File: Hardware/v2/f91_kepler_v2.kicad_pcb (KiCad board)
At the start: 2 copper layers, 30 x 28 mm, 89 parts, among them J1 LS013B7DH03 FPC, Q1 FS8205A, SW1 BTN1/BSL, SW2 BTN2, SW3 BTN3, U1 CC2652R7RGZ, U2 BQ51050B, U3 DW01A, U4 XC6206P302MR, U5 LIS2DW12, U6 DRV2605L, U7 ST25DV04K, Y1 48MHz FA-128, Y2 32.768kHz FC-135

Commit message: feat(hw/v2): geometry-driven placement engine — 0 copper shorts
Replace the fix2..fix5 hand-coordinate approach (could not converge on a
25x27mm / 89-footprint board) with a single authoritative placement engine
that uses real pad geometry headlessly.

Results (kicd-cli DRC, severity-error):
- shorting_items      78 -> 0
- solder_mask_bridge  88 -> 0
- copper_edge_clearance 7 -> 0
- inter-footprint clearance -> 0
- pad-bbox overlaps   90 -> 0
Remaining (non-fab-blocking): 12 intra-footprint clearance (U5 LGA + FL1
balun pins, part-intrinsic), 114 courtyards_overlap (informational),
202 unconnected (routing not started).

Engine: pin FIXED parts (MCU, LCD, edge buttons, antenna, battery, pogo
row), place movable ICs largest-first at nearest-free slot to a home hint,
then place each passive at the nearest-free slot to its home IC's final
position. Collision-tested vs real pad bboxes; rounded-corner clearance via
rect-vs-ring test (KiCad measures arc clearance against the full r2 circle).

tools/overlaps.py: ground-truth pad-bbox overlap checker.
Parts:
- moved C40 414.8 mm to (12.6, 1.30)
- moved C39 410.4 mm to (6.80, 2.55), turned to 90 degrees
- moved TP16 401.1 mm to (1.30, 20.1), turned to 90 degrees
- moved R14 393.4 mm to (2.80, 25.1), turned to 90 degrees
- moved TP15 387.5 mm to (5.55, 23.6), turned to 90 degrees
- moved R12 385.7 mm to (1.80, 18.1), turned to 90 degrees
- moved TP14 385.6 mm to (6.30, 10.6), turned to 90 degrees
- moved R13 385.5 mm to (1.80, 24.6), turned to 90 degrees
- moved J1 385.2 mm to (12.5, 4.50), turned to 180 degrees
- moved C38 381.9 mm to (5.80, 6.55), turned to 90 degrees
- moved TP13 378.9 mm to (2.80, 12.8), turned to 90 degrees
- moved C36 368.7 mm to (2.30, 2.55), turned to 90 degrees
- moved C35 361.4 mm to (1.30, 2.05), turned to 90 degrees
- moved C37 356.2 mm to (16.6, 18.1)
- moved U7 355.2 mm to (9.30, 20.1)
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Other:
- board size 30 x 28 mm -> 25 x 27 mm

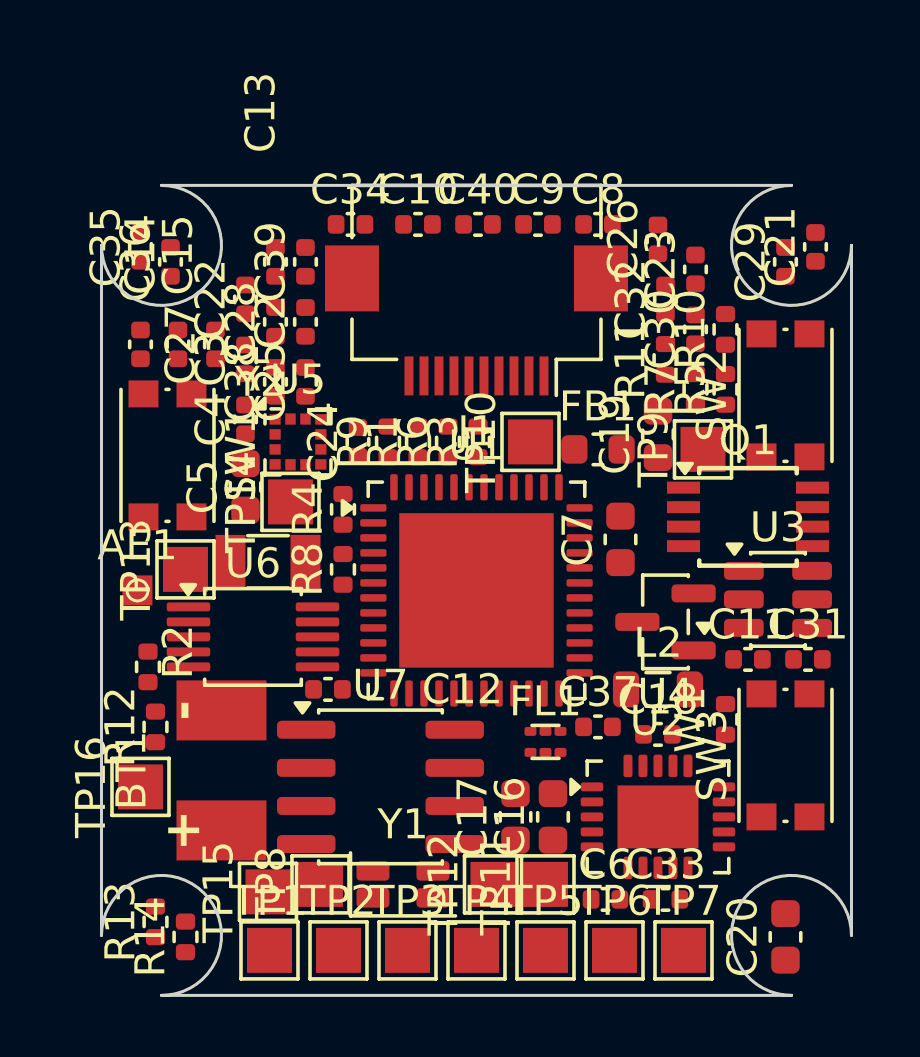
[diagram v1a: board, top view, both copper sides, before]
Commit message: feat(hw/v2): connectivity-aware placement optimizer — 30% less wirelength
Extend place_engine.py with force-directed refinement: each pass pulls every
movable part toward the centroid of its signal-net neighbours (power/ground
nets excluded — they get poured), re-places collision-free, and keeps the
lowest-wirelength layout that still places all 89 parts. Annealed pull
strength (alpha 0.6->0.12) with 0-fail acceptance; board saved on each
accepted best.

Result: signal HPWL 857 -> 597 (-30%), all 89 placed, DRC still clean of
fab-blockers (0 shorts / 0 edge / 0 inter-part clearance). Remaining 12
clearance are intra-footprint (U5 LGA + FL1 balun), 117 courtyards_overlap
informational.
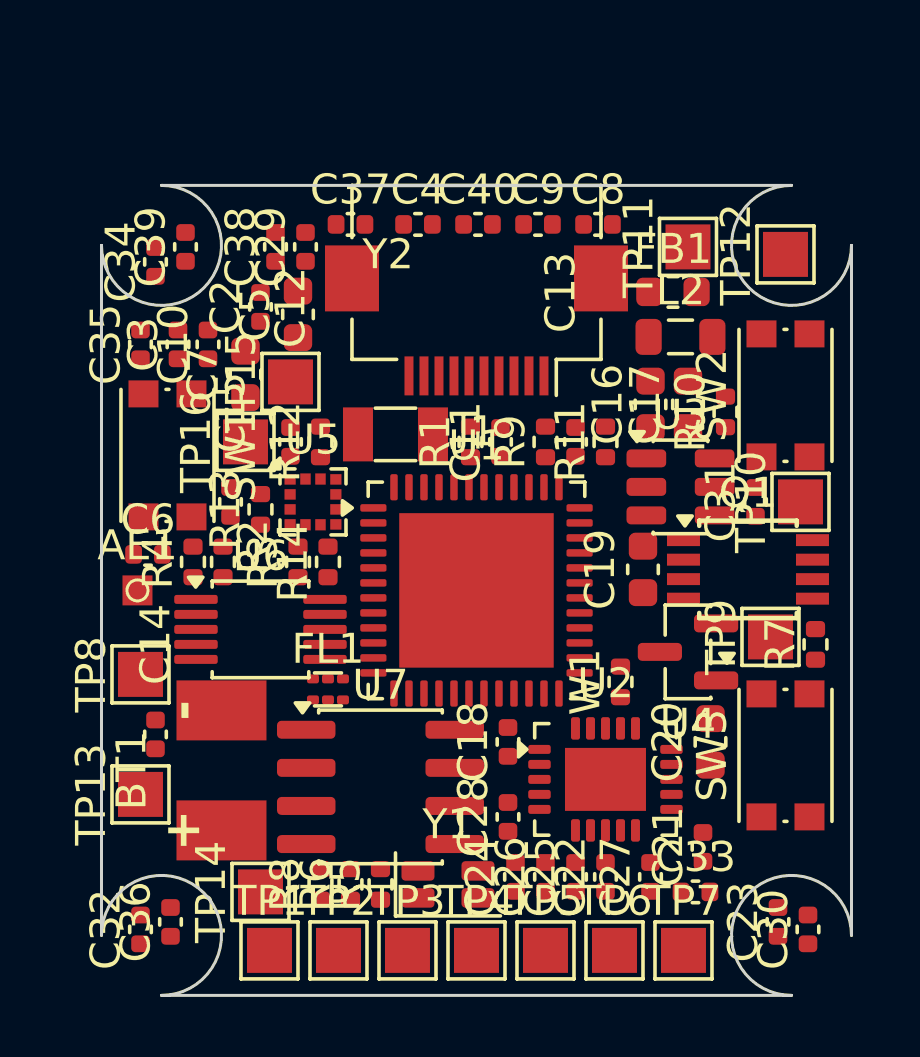
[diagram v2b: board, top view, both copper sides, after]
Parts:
- moved C32 27.3 mm to (1.30, 24.8)
- moved TP12 23.2 mm to (22.8, 2.30)
- moved C27 22.9 mm to (18.3, 23.1)
- moved C22 22.7 mm to (16.8, 23.1)
- moved C36 22.0 mm to (2.30, 24.6)
- moved C23 21.9 mm to (22.6, 24.6)
- moved TP11 21.8 mm to (19.6, 2.05)
- moved C26 21.6 mm to (14.8, 23.1)
- moved C21 20.3 mm to (20.1, 22.1)
- moved C30 20.3 mm to (23.6, 24.8)
- moved R5 20.1 mm to (9.30, 23.3)
- moved C6 19.1 mm to (1.55, 12.3)
- moved C25 18.8 mm to (15.8, 23.1)
- moved C37 18.7 mm to (8.30, 1.30)
- moved C28 18.2 mm to (13.6, 21.1)
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
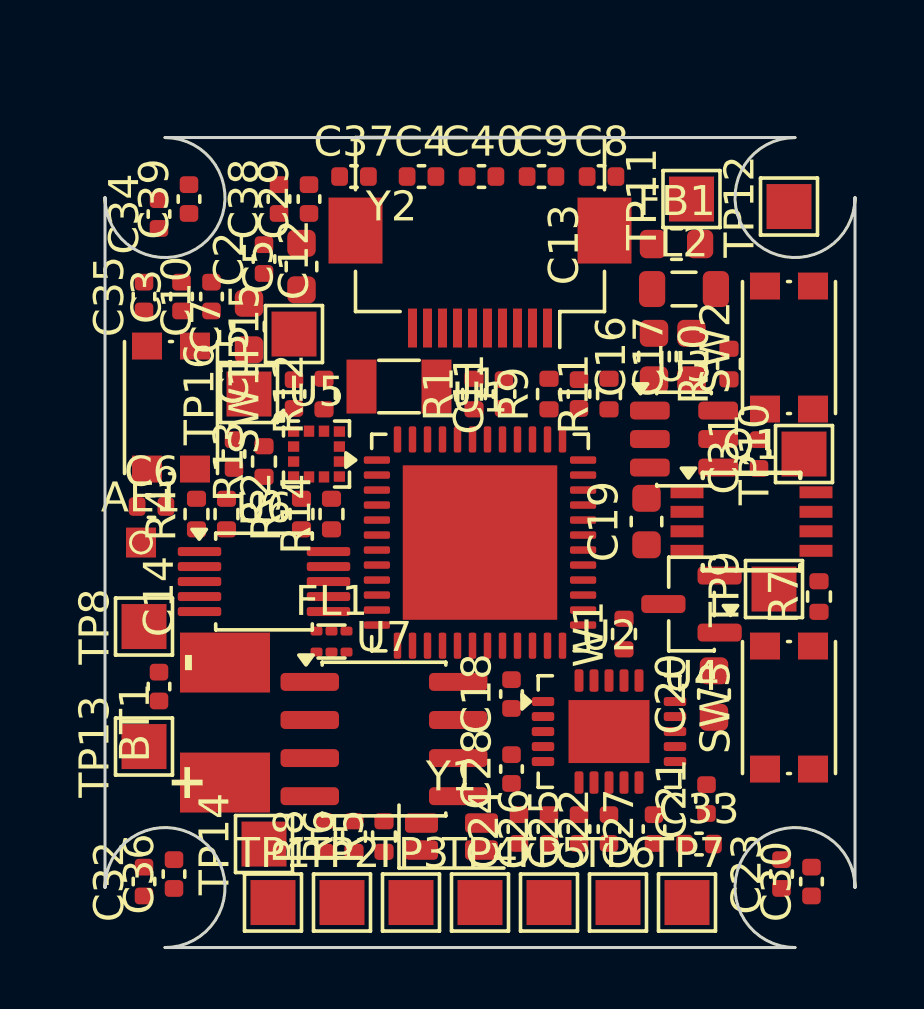
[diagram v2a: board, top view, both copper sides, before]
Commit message: feat(hw/v2): RF-lock balun + series-R for short diff pair
FL1 balun was 6 mm below U1's RF pins (RF_P/RF_N), forcing a long, zigzag
2.4 GHz differential run. Lock FL1 at (7.4,10.9) rot270 — hugging U1 RF_P@
(9.06,10.75)/RF_N@(9.06,11.25), polarity matched so the pair doesn't cross —
and R2 (0R series) at (5.0,12.0) on the straight U1->antenna path to AE1.

Diff-pair length 6 mm -> RF_P 2.04 mm / RF_N 1.32 mm. FL1/R2 excluded from
the force-directed drift (RF correctness over global wirelength: HPWL 597->
682, still -20% vs original 857). DRC clean: 0 shorts / 0 edge / 0 inter-part.
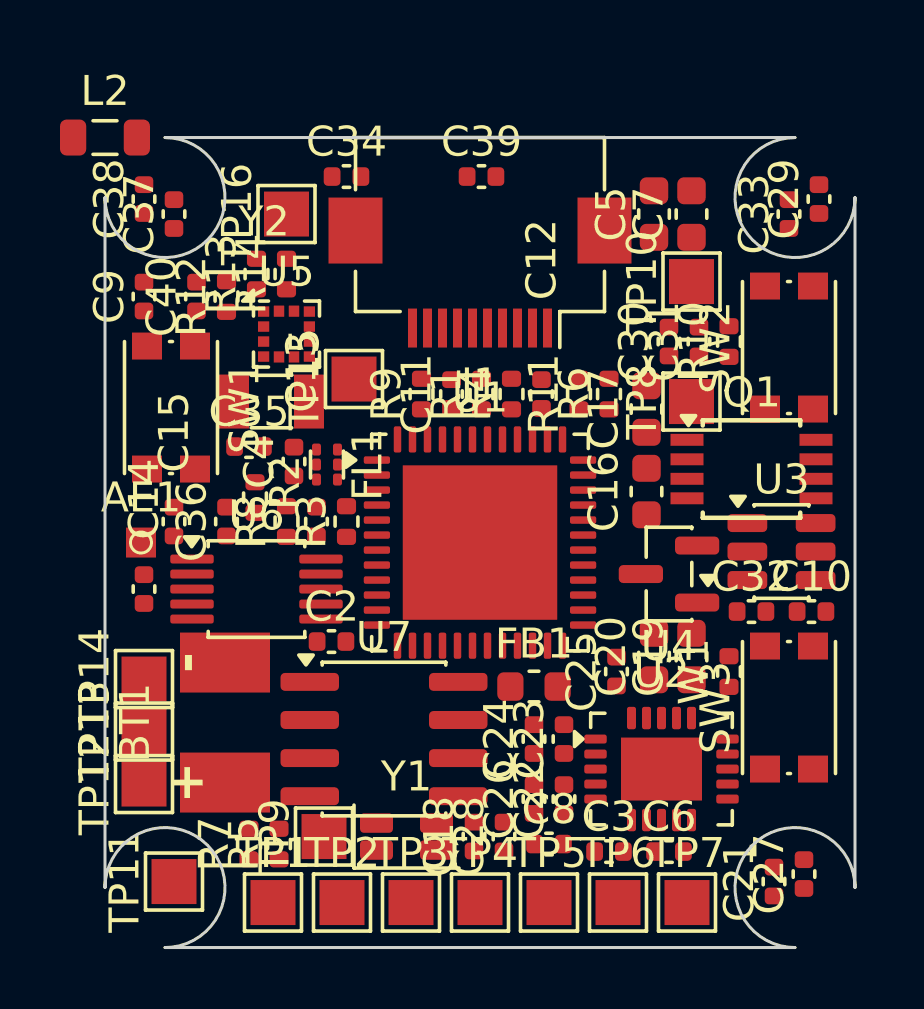
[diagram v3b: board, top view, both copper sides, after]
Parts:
- moved TP12 28.9 mm to (1.30, 21.6)
- moved TP11 28.6 mm to (2.30, 24.8)
- moved C3 23.4 mm to (16.8, 23.8), turned to 0 degrees
- moved C10 22.6 mm to (23.6, 15.8), turned to 0 degrees
- moved C8 22.3 mm to (14.8, 23.6)
- moved C32 22.2 mm to (21.6, 15.8), turned to 0 degrees
- moved C33 21.2 mm to (22.8, 2.55), turned to 90 degrees
- moved C6 20.7 mm to (18.8, 23.8)
- moved R7 20.7 mm to (4.80, 23.6)
- moved L2 19.9 mm to (0.00, 0.00)
- moved TP8 19.7 mm to (19.6, 8.80)
- moved C30 18.6 mm to (18.8, 6.80)
- moved TP9 17.1 mm to (7.30, 23.3)
- moved R6 17.0 mm to (16.8, 8.55)
- moved C29 17.0 mm to (23.8, 2.05)
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
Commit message: fix(hw/v2): L2 stranded off-board at origin; lock it to DCDC_SW pin
L2 (DCDC inductor) was sitting at (0,0) — fully off-board, copper at x=-1.5.
Cause: L2's only nets are DCDC_SW + VDDR, both in the power-exclusion set, so
it had 0 signal degree and sorted dead-last; no free slot remained, and
half_extents() parks parts at origin to measure -> a failed placement left it
there. DRC's arc check missed it (copper far from any edge).

Fixes:
- Lock L2 in FIXED at (17.5,12.4) rot90, hugging U1 DCDC_SW pin33 @(15.94,
  12.25): switching-node trace 3.7mm -> 1.98mm. Packer reflows C16/C28 around it.
- place_order(): all SEED ICs place early (not just >=4mm^2), so power-only
  parts can't get starved.
- place_pass(): truly-unplaceable parts parked at their hint (on-board,
  DRC-visible) instead of left at origin.
- End-of-run guard: reload saved board, assert no part off-board.

All 89 on-board. DRC clean: 0 shorts / 0 edge / 0 inter-part. RF diff pair
unchanged (2.04/1.32mm).
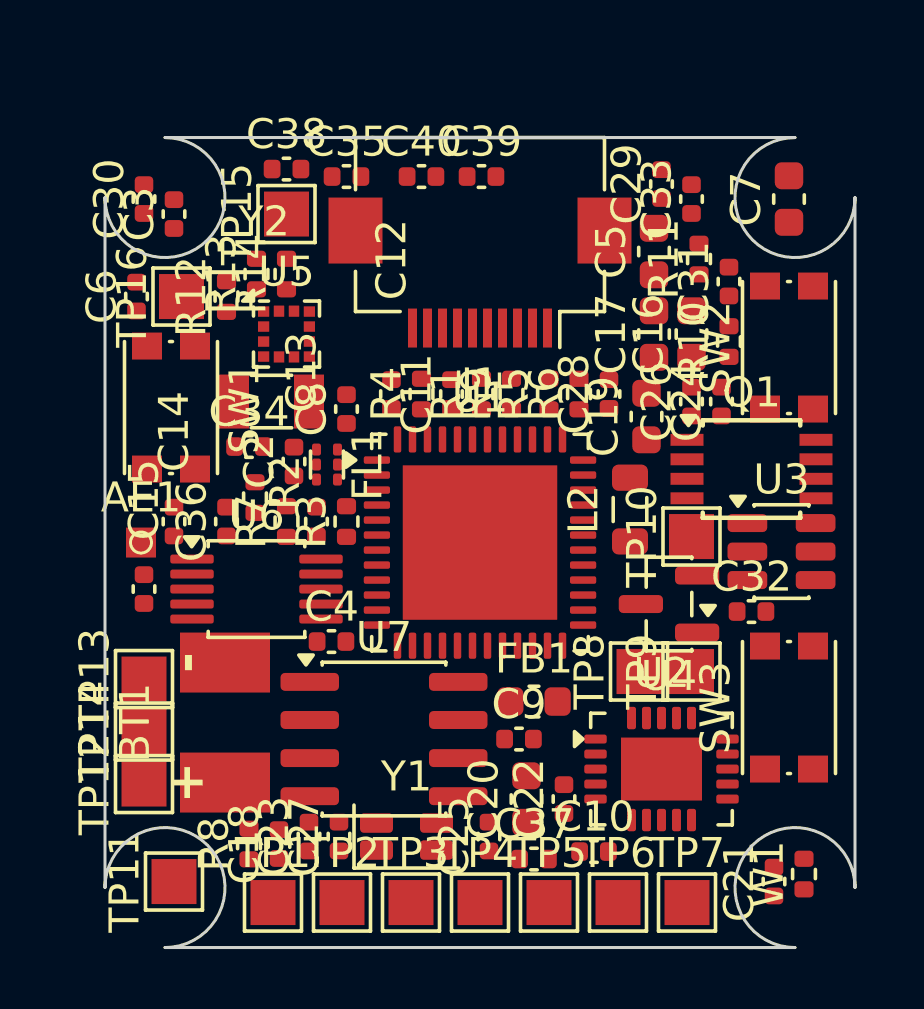
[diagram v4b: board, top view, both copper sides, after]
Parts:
- moved C3 25.7 mm to (2.30, 2.55), turned to 90 degrees
- moved C6 25.6 mm to (1.05, 5.30), turned to 90 degrees
- moved C37 24.6 mm to (14.3, 24.1), turned to 0 degrees
- moved L2 21.4 mm to (17.5, 12.4), turned to 90 degrees
- moved C9 19.3 mm to (13.8, 20.1), turned to 0 degrees
- moved C30 18.1 mm to (1.30, 2.05)
- moved R5 17.5 mm to (14.8, 8.55)
- moved C8 16.0 mm to (8.05, 9.05), turned to 90 degrees
- moved C27 15.6 mm to (7.80, 23.3)
- moved C28 15.2 mm to (16.8, 8.55)
- moved C26 14.3 mm to (19.6, 8.80)
- moved TP9 13.4 mm to (19.6, 17.8)
- moved C24 12.9 mm to (20.6, 8.80)
- moved R7 10.8 mm to (6.05, 12.8)
- moved R8 10.8 mm to (4.80, 23.6)
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
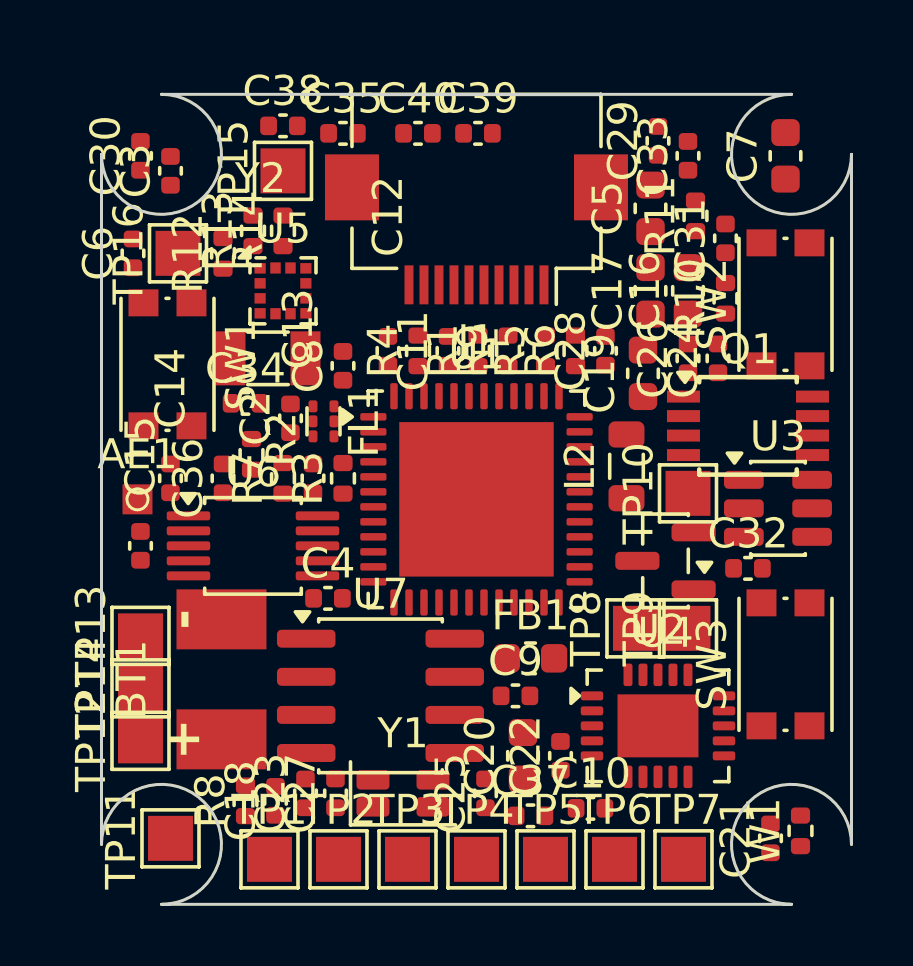
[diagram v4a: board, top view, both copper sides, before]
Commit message: feat(hw/v2): replace PCB IFA with Johanson 2450AT18A100 chip antenna
The v1 IFA could not be ported (original is a round DipTrace board with a
discrete LC match and a different RF front-end; geometry would need full
retuning and could not be cleanly extracted). Switched to a characterized
chip antenna with a vendor reference layout instead.

- New footprint ANT_2450AT18A100 (EIA 1206, 3.2x1.6, pin1=Feed pin2=NC) from
  datasheet 36S0021A Rev4.0.
- antenna_prep.py: swap AE1 IFA feed-pad -> chip antenna, preserve ANT_FEED.
- Placed at the top-left corner on the top edge (frees the left edge for SW1);
  existing R2 + C14/C15 serve as the tee/pi match (retune values on bench).
- antenna_keepout.py: ground-pour keepout rule area (no fill, both layers) at
  the antenna corner per the 6.5mm datasheet clearance.
- place_engine.py: AE1/R2 RF-locked at the corner, antenna near-field
  reservation, SW1/U7 relocated; 89/89 placed, HPWL 624.
- Edge clearance rule 0.5 -> 0.25mm (JLC-fabricable; antenna feed pad sits
  0.291mm from the corner arc on this dense 25x27 board).

DRC: 0 shorts / 0 edge / 0 inter-part clearance. 12 intra-footprint
(U5/FL1) + 116 courtyard are non-blocking.

NOTE: schematic still has AE1 as the 1-pad IFA symbol — needs a schematic
sync (assign chip-antenna symbol/footprint, pin2 NC) before netlist re-import.
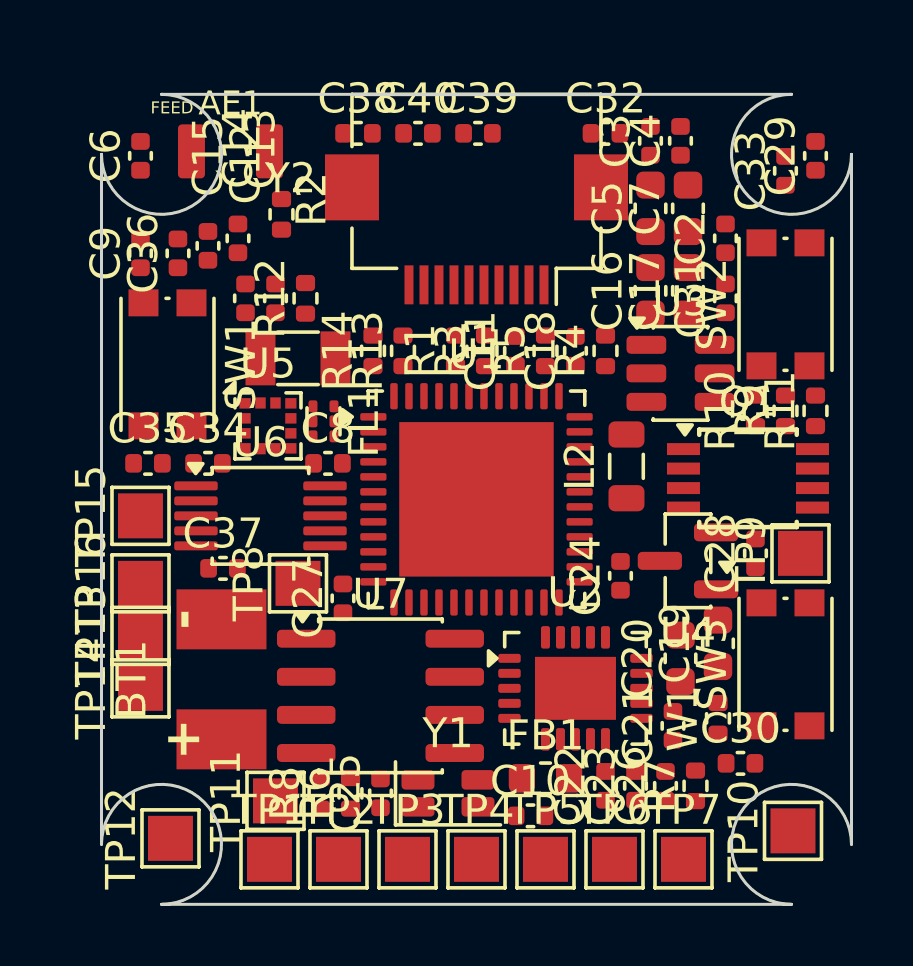
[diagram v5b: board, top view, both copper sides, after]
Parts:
- AE1: value PCB-IFA (v1 geometry) -> 2450AT18A100; footprint ANT_v1_IFA -> ANT_2450AT18A100
- moved C30 28.5 mm to (21.3, 22.3), turned to 0 degrees
- moved C9 19.3 mm to (1.30, 5.30), turned to 90 degrees
- moved C4 19.3 mm to (19.3, 1.55), turned to 90 degrees
- moved C18 18.0 mm to (15.8, 8.55)
- moved R7 17.2 mm to (19.8, 23.1)
- moved R6 16.5 mm to (8.30, 23.3)
- moved C3 16.0 mm to (18.3, 1.55)
- moved C2 15.7 mm to (20.8, 4.80)
- moved C32 15.3 mm to (16.8, 1.30)
- moved C26 14.3 mm to (18.8, 23.1)
- moved C37 13.2 mm to (4.05, 15.8)
- moved C35 12.8 mm to (1.55, 12.3)
- moved TP15 12.4 mm to (1.30, 14.1)
- moved AE1 12.0 mm to (4.30, 1.90)
- moved TP10 11.8 mm to (23.1, 24.6)
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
